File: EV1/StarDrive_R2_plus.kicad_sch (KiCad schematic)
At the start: 45 parts, among them J1 Conn_02x06_Odd_Even, J2 Conn_02x06_Odd_Even, J3 Conn_02x17_Odd_Even, J4 Conn_02x13_Odd_Even, U1 PCF8573P, U2 74HCT74, U3 74HCT04, U4 AM5380, U5 SN74F32, U6 74LS32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

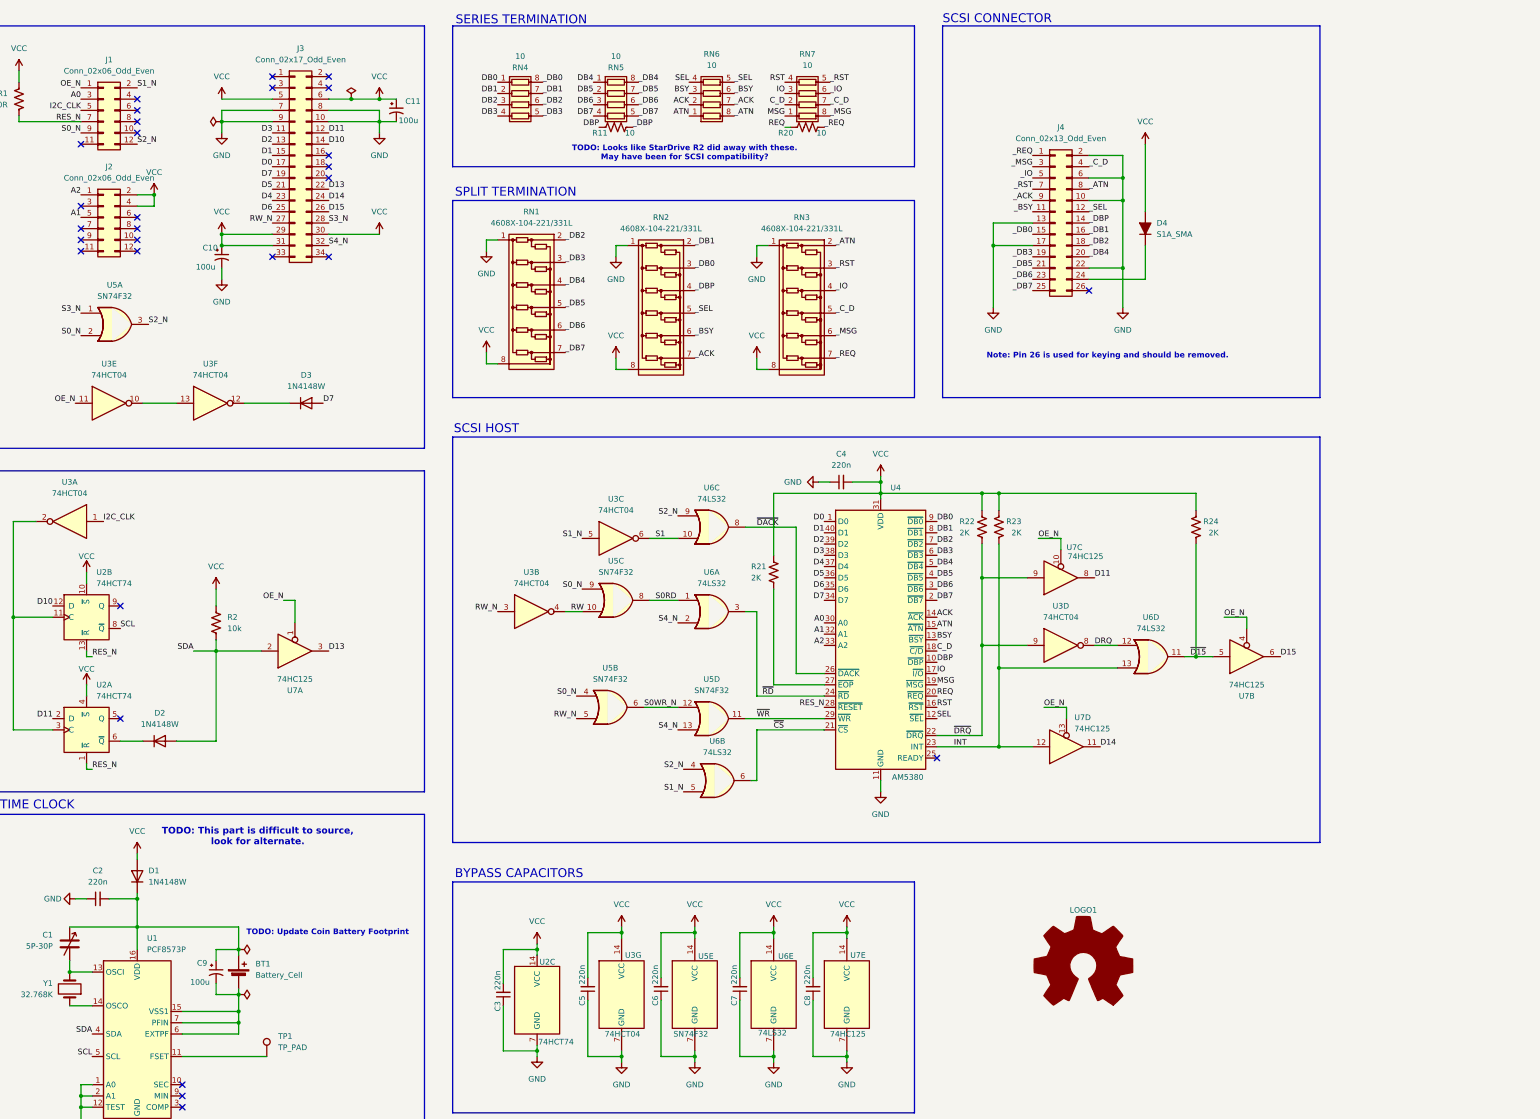
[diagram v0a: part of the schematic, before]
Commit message: Added notes and comments to schematic Added schematic plot
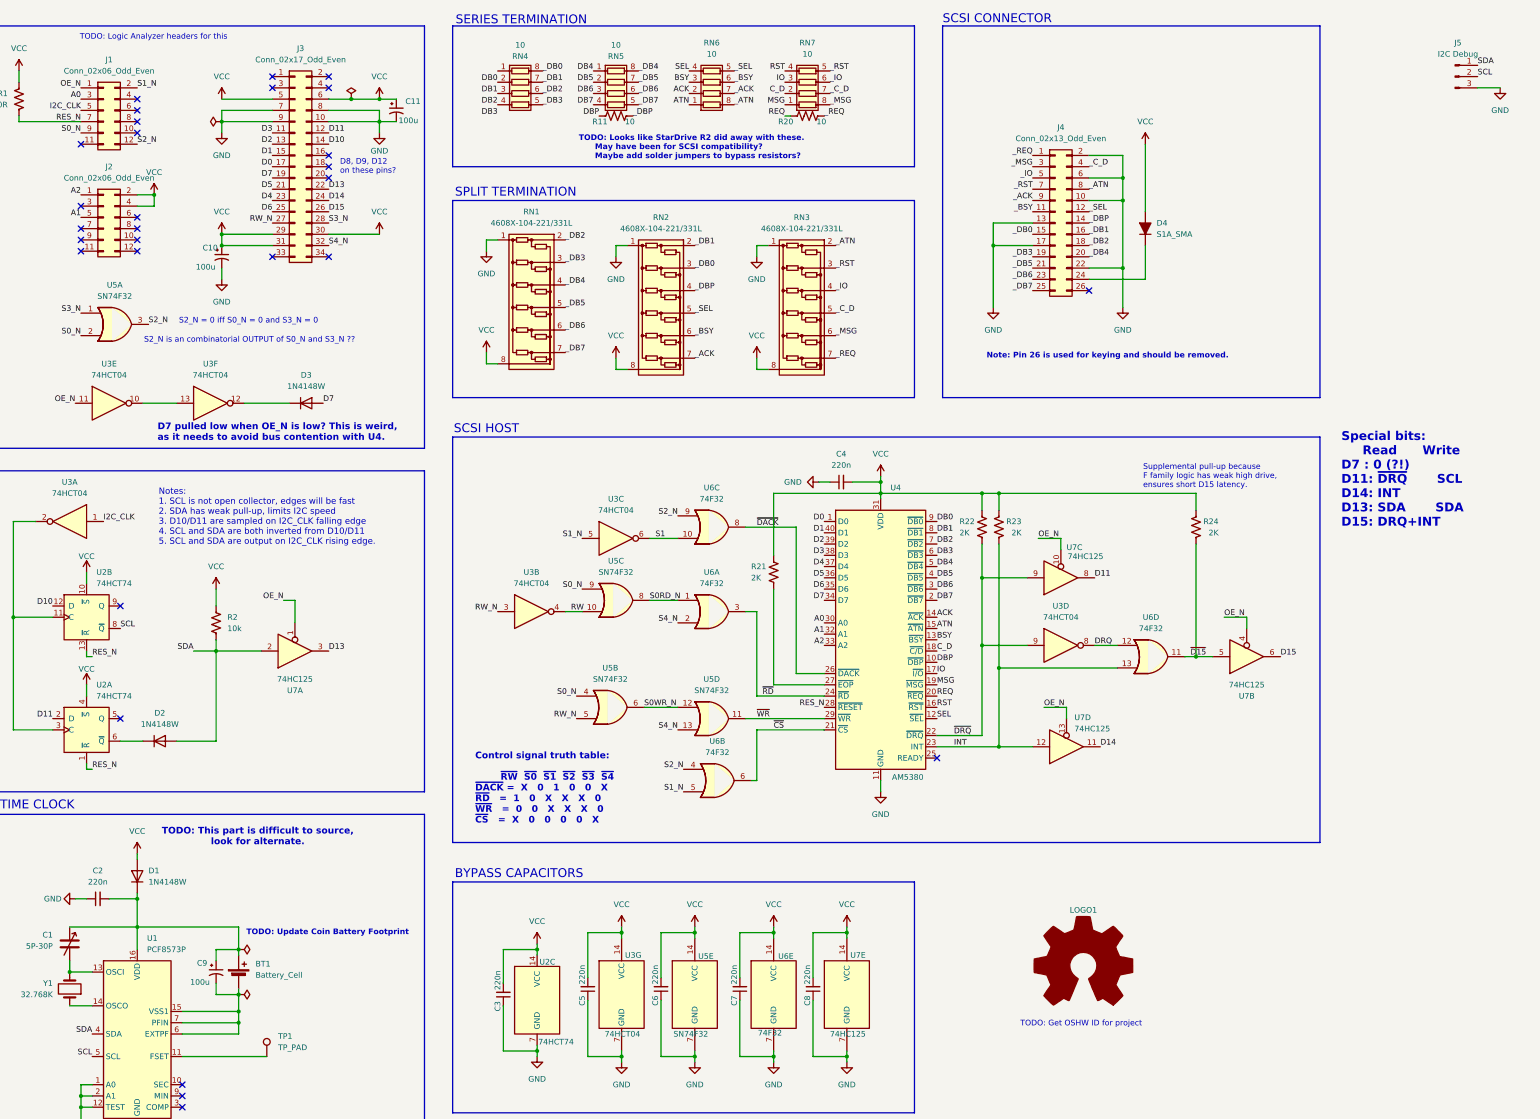
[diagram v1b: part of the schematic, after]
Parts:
- added J5: I2C Debug, symbol Connector:Conn_01x03_Pin
- U6: value 74LS32 -> 74F32
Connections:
- net DB0: now also RN4.2 (R2.1); no longer RN4.1 (R1.1)
- net DB1: now also RN4.3 (R3.1); no longer RN4.2 (R2.1)
- net DB2: now also RN4.4 (R4.1); no longer RN4.3 (R3.1)
- net DB3: no longer RN4.4 (R4.1)
- net GND: now also J5.3 (Pin_3)
- net SCL: now also J5.2 (Pin_2)
- net SDA: now also J5.1 (Pin_1)
- net S0RD renamed S0RD_N
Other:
- note added: "Control signal truth table: ~{RW} ~{S0} ~{S1} ~{S2} ~{S3} ~{S4} ~{DACK} = X 0 1 0 0 X ~{RD} = 1 0 X X X 0 ~{WR} = 0 0 X X X 0 ~{CS} = X 0 0 0 0 X"
- note added: "D7 pulled low when OE_N is low? This is weird, as it needs to avoid bus contention with U4."
- note added: "D8, D9, D12 on these pins?"
- note added: "Notes: 1. SCL is not open collector, edges will be fast 2. SDA has weak pull-up, limits I2C speed 3. D10/D11 are sampled on I2C_CLK falling edge 4. SCL and SDA are both inverted from D10/D11 5. SCL and SDA are output on I2C_CLK rising edge."
- note added: "S2_N = 0 iff S0_N = 0 and S3_N = 0"
- note added: "S2_N is an combinatorial OUTPUT of S0_N and S3_N ??"
- note added: "Special bits: Read Write D7 : 0 (?!) D11: ~{DRQ} SCL D14: INT D13: SDA SDA D15: DRQ+INT"
- note added: "Supplemental pull-up because F family logic has weak high drive, ensures short D15 latency."
- note added: "TODO: Get OSHW ID for project"
- note added: "TODO: Logic Analyzer headers for this"
- note added: "TODO: Looks like StarDrive R2 did away with these. May have been for SCSI compatibility? Maybe add solder jumpers to bypass resistors?"
- note removed: "TODO: Looks like StarDrive R2 did away with these. May have been for SCSI compatibility?"
- moved on the sheet: R11, R20, RN4, RN5, RN6, RN7

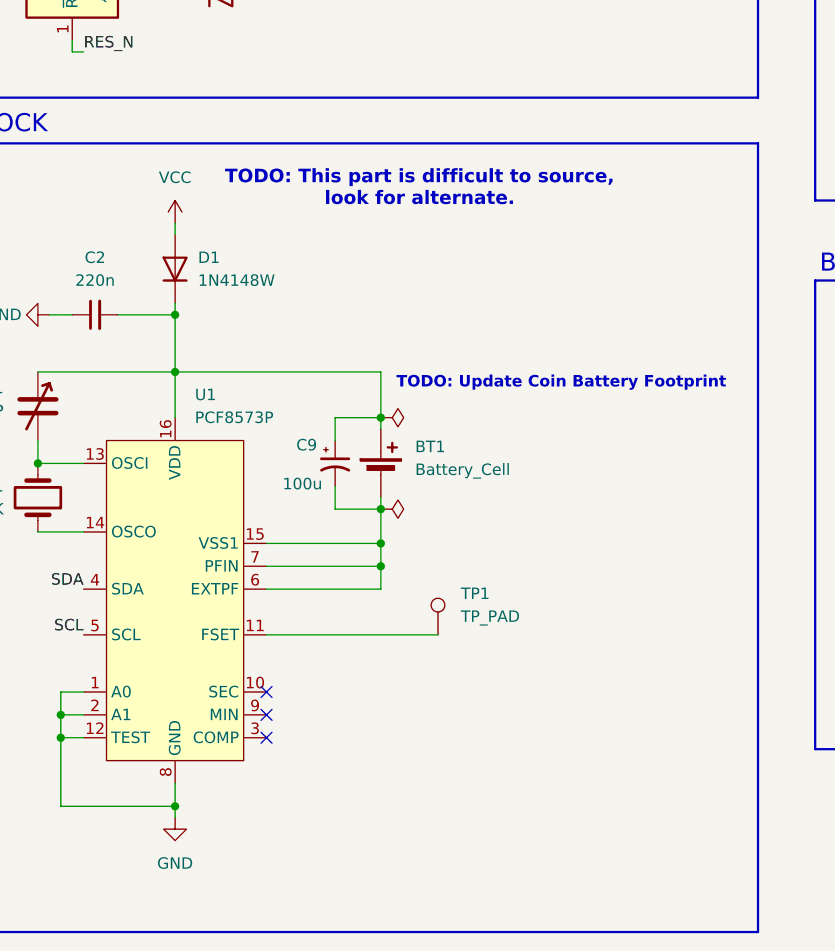
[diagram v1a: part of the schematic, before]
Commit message: Updated header locations
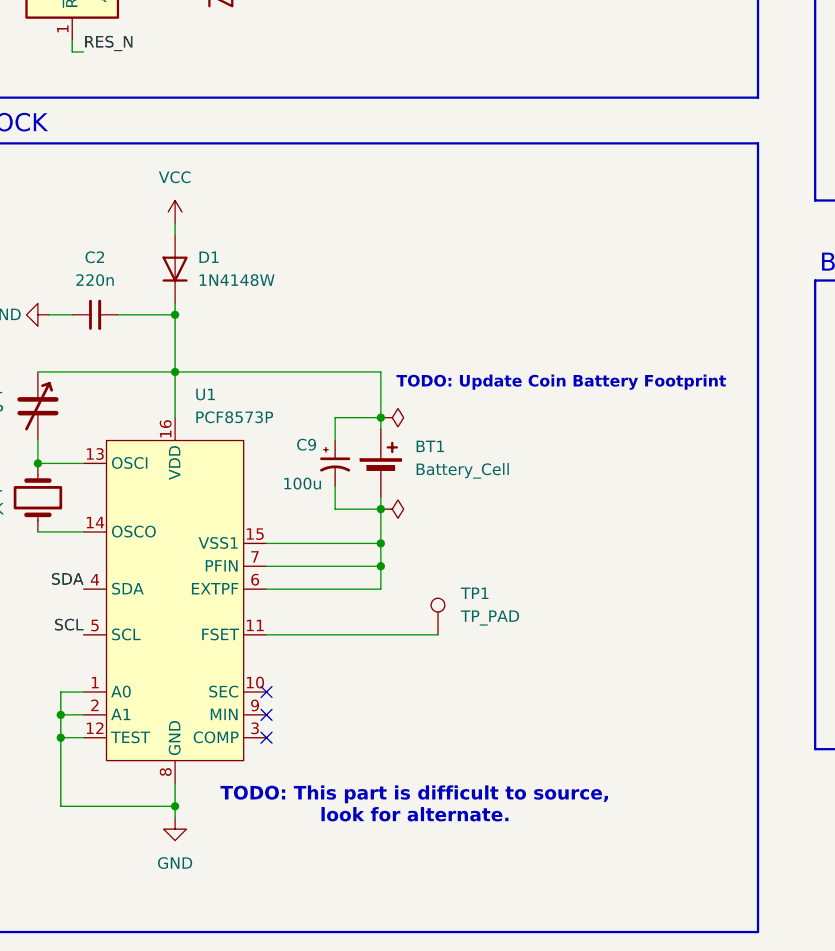
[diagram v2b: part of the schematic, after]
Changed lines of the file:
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@@
 	(text "TODO: This part is difficult to source,\nlook for alternate."
 		(exclude_from_sim no)
-		(at 83.058 198.12 0)
+		(at 82.55 266.7 0)
 		(effects
 			(font

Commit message: First prototype Gerber out
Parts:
- removed J5: I2C Debug, symbol Connector:Conn_01x03_Pin
- added D5: 1N4148W, Diode_SMD:D_SOD-123, symbol Diode:1N4148W
- added J5: DBG1, Connector_PinHeader_2.54mm:PinHeader_1x05_P2.54mm_Vertical, symbol Connector:Conn_01x05_Pin
- added JP1: VBAT_GND, Jumper:SolderJumper-2_P1.3mm_Open_Pad1.0x1.5mm, symbol Jumper:SolderJumper_2_Open
- added U8: PCF8573P, Package_SO:SOIC-16W_7.5x10.3mm_P1.27mm, symbol StarDrive_R2_symsch:PCF8573P
- BT1: footprint Battery:Battery_Panasonic_CR2032-HFN_Horizontal_CircularHoles -> ZZZ_ProjectLibrary:AliEx_BatClip
- D2, D3: footprint Diode_SMD:D_SOD-123 -> Diode_SMD:D_SOD-323_HandSoldering
- RN4, RN5, RN6, RN7: value 10 -> CAY16-10R0F4LF
- TP1: value TP_PAD -> FSET
- U3, U5, U6, U7: footprint Package_SO:SO-14_3.9x8.65mm_P1.27mm -> Package_SO:SOIC-14_3.9x8.7mm_P1.27mm
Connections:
- net DB0: now also RN4.1 (R1.1); no longer RN4.2 (R2.1)
- net DB1: now also RN4.2 (R2.1); no longer RN4.3 (R3.1)
- net DB2: now also RN4.3 (R3.1); no longer RN4.4 (R4.1)
- net DB3: now also RN4.4 (R4.1)
- net GND: now also J5.5 (Pin_5), JP1.1 (A), U8.1 (A0), U8.12 (TEST), U8.2 (A1), U8.8 (GND)
- net SCL: now also J5.2 (Pin_2), U8.5 (SCL)
- net SDA: now also J5.3 (Pin_3), U8.4 (SDA)
- net RTC_VDD: now reaches C1.1, C2.2, D1.1 (K), U1.16 (VDD)
- net RTC_VDD: now also D5.1 (K), J5.4 (Pin_4), U8.16 (VDD); no longer BT1.1 (+), C9.1
- net OSCI: now reaches C1.2, U1.13 (OSCI), Y1.2
- net OSCI: now also J5.1 (Pin_1), U8.13 (OSCI)
- net VBAT_GND: now reaches BT1.2 (-), C9.2, U1.15 (VSS1), U1.6 (EXTPF), U1.7 (PFIN)
- net VBAT_GND: now also JP1.2 (B), U8.15 (VSS1), U8.6 (EXTPF), U8.7 (PFIN)
- net OSCO: now reaches U1.14 (OSCO), Y1.1
- net OSCO: now also U8.14 (OSCO)
- net FSET: now reaches TP1.1, U1.11 (FSET)
- net FSET: now also U8.11 (FSET)
- new net: BT1.1 (+), C9.1, D5.2 (A)
- no-connect marks 29 -> 32
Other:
- note added: "TODO: PCF8573 is difficult to source, look for alternate."
- note added: "TODO: Verify coin cell battery works here."
- note removed: "TODO: This part is difficult to source, look for alternate."
- note removed: "TODO: Update Coin Battery Footprint"
- moved on the sheet: C3, C4, C5, C6, C7, C8, LOGO1, R21, R22, R23, R24, TP1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
